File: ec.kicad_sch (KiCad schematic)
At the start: 51 parts, among them IC1 ADUM6010ARSZ, J1 EC, J2 Temperature, U1 ADuM1250, U2 ADS1115IDGS, U4 TPS60400DBV, U5 LM324, U6 MCP4017T-502E/LT

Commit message: Add title to all schematics pages
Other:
- title: (none) -> EC
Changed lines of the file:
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@@
 	(paper "A4")
 	(title_block
+		(title "EC")
 		(rev "1")
 	)

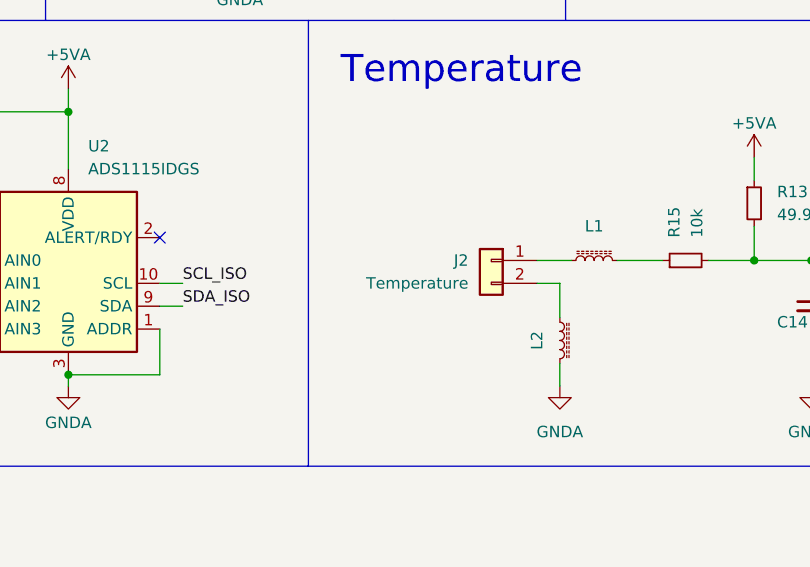
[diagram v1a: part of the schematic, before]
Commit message: Redesign board to fit within 102mm x 102mm
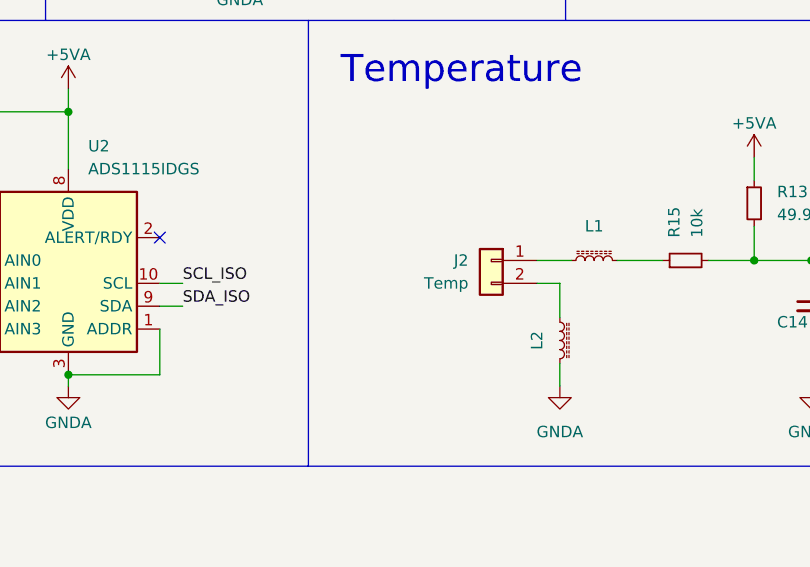
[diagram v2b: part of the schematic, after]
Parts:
- IC1, R1, U1, U2, U4: now left out of the parts list
- J2: value Temperature -> Temp
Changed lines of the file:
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@@
 		(unit 1)
 		(exclude_from_sim no)
-		(in_bom yes)
+		(in_bom no)
 		(on_board yes)
 		(dnp no)
@@
 		(unit 1)
 		(exclude_from_sim no)
-		(in_bom yes)
+		(in_bom no)
 		(on_board yes)
 		(dnp no)
@@
 		(unit 1)
 		(exclude_from_sim no)
-		(in_bom yes)
+		(in_bom no)
 		(on_board yes)
 		(dnp no)
@@
 		(unit 1)
 		(exclude_from_sim no)
-		(in_bom yes)
+		(in_bom no)
 		(on_board yes)
 		(dnp no)
@@
 			)
 		)
-		(property "Value" "Temperature"
+		(property "Value" "Temp"
 			(at 195.58 105.4099 0)
 			(effects
@@
 		(unit 1)
 		(exclude_from_sim no)
-		(in_bom yes)
+		(in_bom no)
 		(on_board yes)
 		(dnp no)

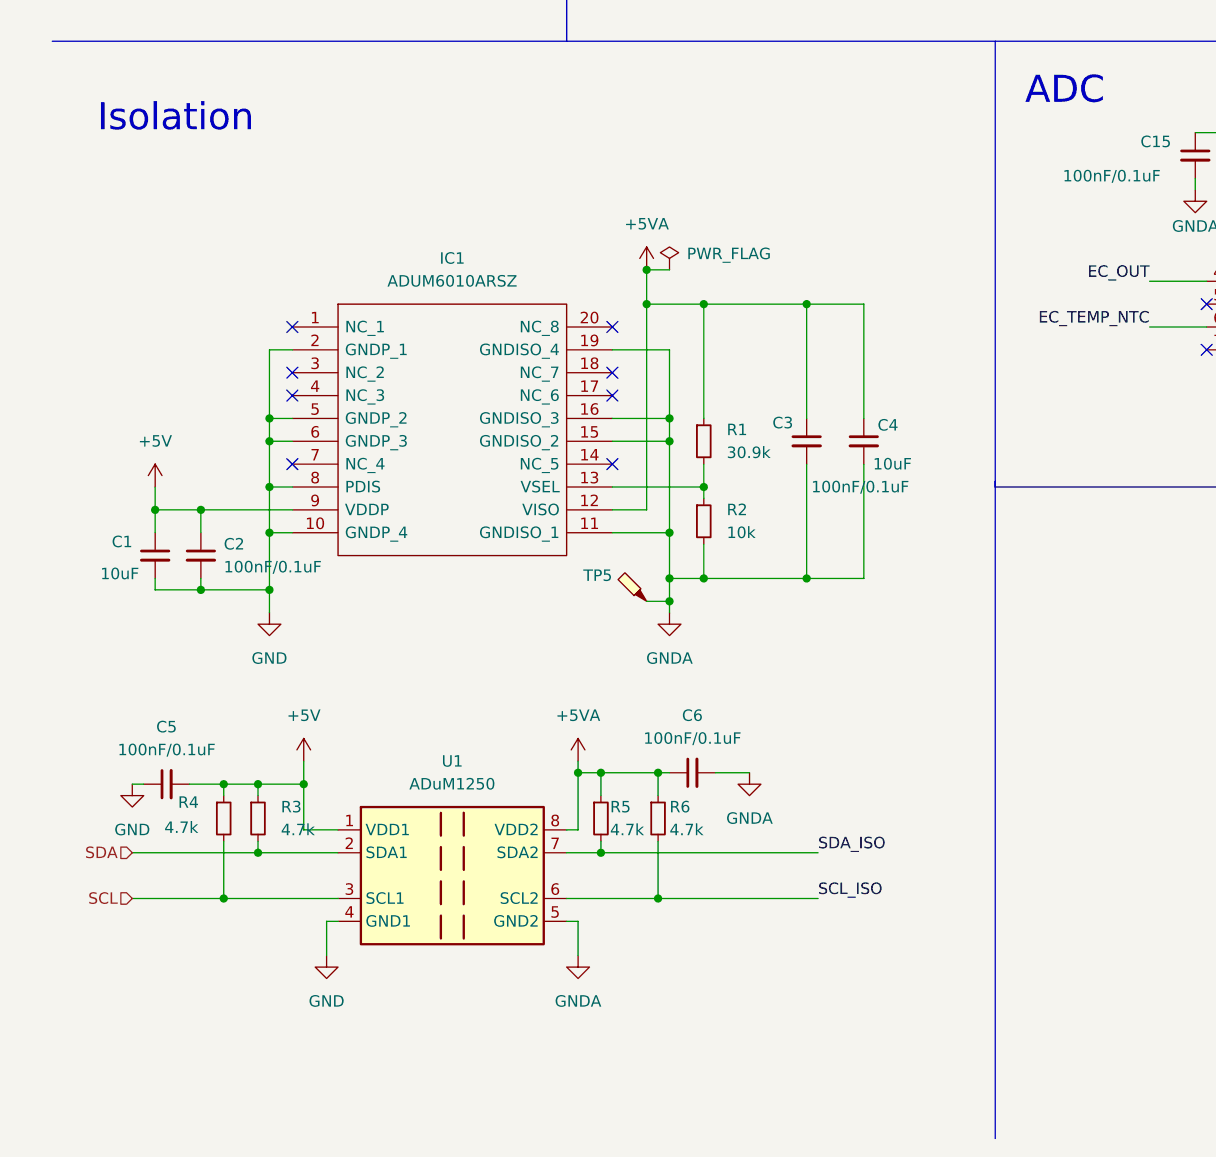
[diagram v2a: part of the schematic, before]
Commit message: Switch isolators to ADM3260
Change EC isolator.
See #1
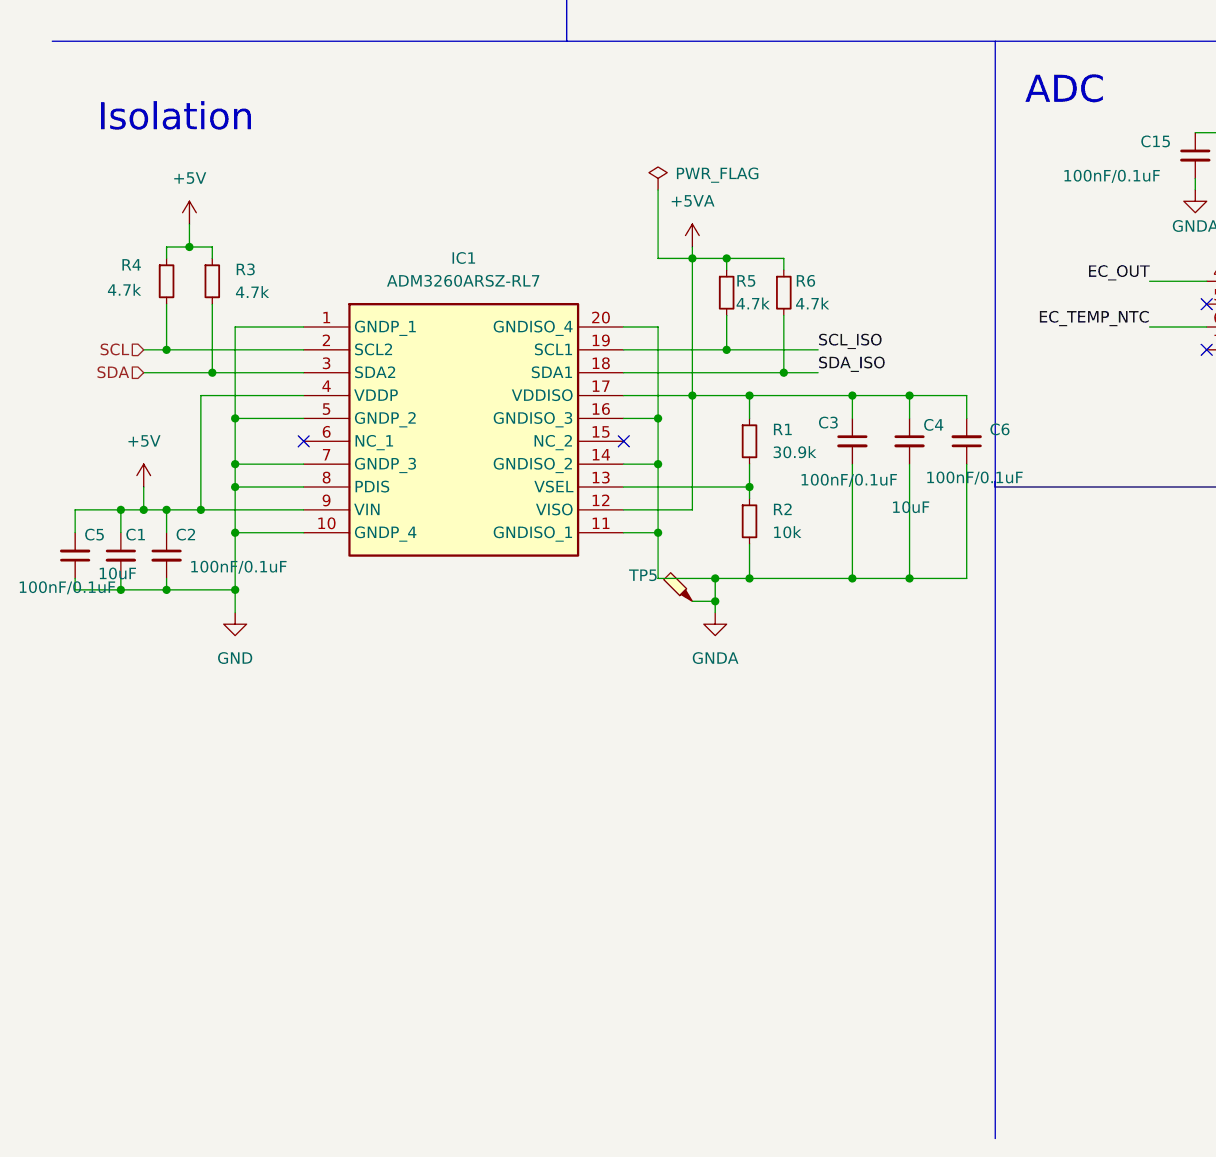
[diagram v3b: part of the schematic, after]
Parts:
- removed IC1: ADUM6010ARSZ, HydroponicFlowerControl:ADUM6010, symbol HydroponicFlowerControl:ADUM6010ARSZ
- removed U1: ADuM1250, Package_SO:SOIC-8_3.9x4.9mm_P1.27mm, symbol Isolator:ADuM1250
- added IC1: ADM3260ARSZ-RL7, HydroponicFlowerControl:SOP65P780X200-20N, symbol HydroponicFlowerControl:ADM3260ARSZ-RL7
- U6: JLCPCB Rotation Offset (none) -> -90
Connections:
- net +5V: now also IC1.4 (VDDP), IC1.9 (VIN)
- net +5VA: now also C6.2, IC1.12 (VISO), IC1.17 (VDDISO); no longer C6.1
- net GND: now also IC1.1 (GNDP_1), IC1.10 (GNDP_4), IC1.5 (GNDP_2), IC1.7 (GNDP_3), IC1.8 (PDIS)
- net GNDA: now also C6.1, IC1.11 (GNDISO_1), IC1.14 (GNDISO_2), IC1.16 (GNDISO_3), IC1.20 (GNDISO_4); no longer C6.2
- net SCL: now also IC1.2 (SCL2)
- net SCL_ISO: now also R5.2, IC1.19 (SCL1); no longer R6.2
- net SDA: now also IC1.3 (SDA2)
- net SDA_ISO: now also R6.2, IC1.18 (SDA1); no longer R5.2
- net at R1.2, R2.1: now also IC1.13 (VSEL)
- no-connect marks 11 -> 5
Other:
- moved on the sheet: C1, C2, C3, C4, C5, C6, R1, R2, R3, R4, R5, R6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

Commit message: Add disable signals for ec and ph
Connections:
- net GND: no longer IC1.8 (PDIS)
- new net DISABLE: IC1.8 (PDIS)
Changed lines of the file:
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@@
-	)
-	(junction
-		(at 33.02 125.73)
-		(diameter 0)
-		(color 0 0 0 0)
 	)
 	(junction
@@
 	(wire
 		(pts
-			(xy 33.02 125.73) (xy 33.02 130.81)
+			(xy 33.02 123.19) (xy 33.02 130.81)
 		)
 		(stroke
@@
 	(wire
 		(pts
-			(xy 33.02 125.73) (xy 40.64 125.73)
-		)
-		(stroke
-			(width 0)
-			(type default)
-		)
-	)
-	(wire
-		(pts
 			(xy 40.64 107.95) (xy 33.02 107.95)
 		)
@@
 		(pts
 			(xy 25.4 110.49) (xy 40.64 110.49)
-		)
-		(stroke
-			(width 0)
-			(type default)
-		)
-	)
-	(wire
-		(pts
-			(xy 33.02 123.19) (xy 33.02 125.73)
 		)
 		(stroke
@@
 		(fields_autoplaced yes)
 		(effects
+			(font
+				(size 1.27 1.27)
+			)
+			(justify right)
+		)
+	)
+	(hierarchical_label "DISABLE"
+		(shape input)
+		(at 40.64 125.73 180)
+		(fields_autoplaced yes)
+		(effects

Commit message: Fix manufaturing properties
Such as rotations
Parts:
- IC1, U2: JLCPCB Rotation Offset (none) -> 270; now in the parts list
- R1, U4: now in the parts list
- U6: JLCPCB Rotation Offset -90 -> 90
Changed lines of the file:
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@@
 		(unit 1)
 		(exclude_from_sim no)
-		(in_bom no)
+		(in_bom yes)
 		(on_board yes)
 		(dnp no)
@@
 			)
 		)
+		(property "JLCPCB Rotation Offset" "270"
+			(at 151.13 105.41 0)
+			(effects
+				(font
+					(size 1.27 1.27)
+				)
+				(hide yes)
+			)
+		)
 		(pin "3"
 		)
@@
 		(unit 1)
 		(exclude_from_sim no)
-		(in_bom no)
+		(in_bom yes)
 		(on_board yes)
 		(dnp no)
@@
 			)
 		)
+		(property "JLCPCB Rotation Offset" "270"
+			(at 40.64 107.95 0)
+			(effects
+				(font
+					(size 1.27 1.27)
+				)
+				(hide yes)
+			)
+		)
 		(pin "17"
 		)
@@
 		(unit 1)
 		(exclude_from_sim no)
-		(in_bom no)
+		(in_bom yes)
 		(on_board yes)
 		(dnp no)
@@
 		(unit 1)
 		(exclude_from_sim no)
-		(in_bom no)
+		(in_bom yes)
 		(on_board yes)
 		(dnp no)
@@
 			)
 		)
-		(property "JLCPCB Rotation Offset" "-90"
+		(property "JLCPCB Rotation Offset" "90"
 			(at 172.72 62.23 0)
 			(effects

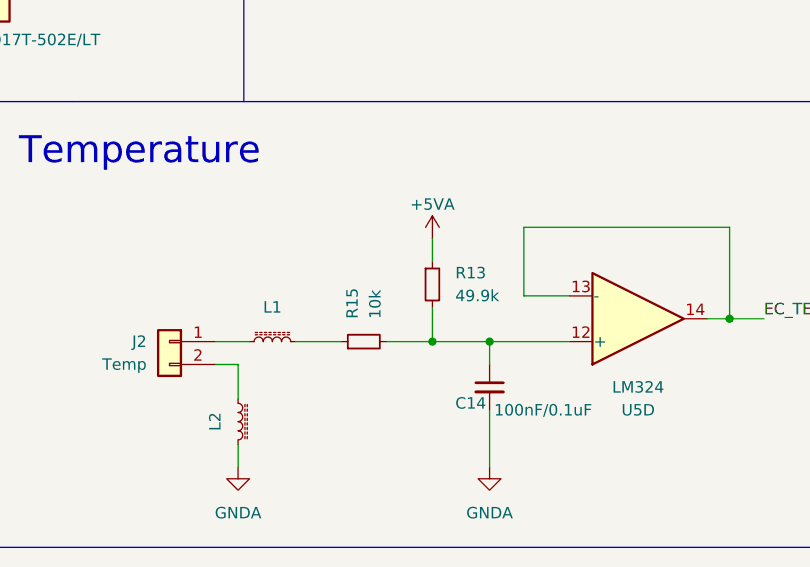
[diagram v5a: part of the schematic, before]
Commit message: Move R15 and R48 to the right side of the divider
Closes #6
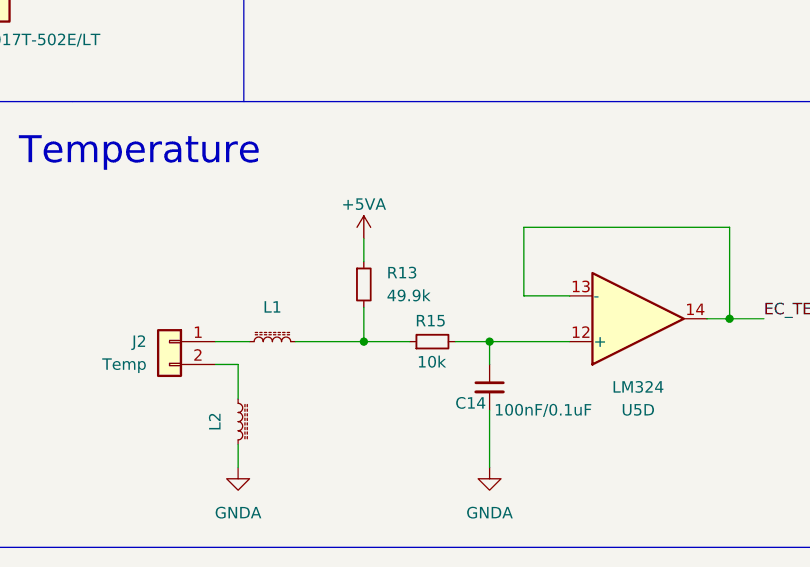
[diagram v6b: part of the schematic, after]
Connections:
- net at L1.2, R15.1: now also R13.2
- net at C14.1, R15.2, U5.12 (+): no longer R13.2
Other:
- moved on the sheet: R13, R15
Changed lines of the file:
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@@
 	)
 	(junction
+		(at 219.71 102.87)
+		(diameter 0)
+		(color 0 0 0 0)
+	)
+	(junction
 		(at 93.98 113.03)
 		(diameter 0)
@@
 	)
 	(junction
-		(at 227.33 102.87)
-		(diameter 0)
-		(color 0 0 0 0)
-	)
-	(junction
 		(at 245.11 41.91)
 		(diameter 0)
@@
 	(wire
 		(pts
-			(xy 227.33 102.87) (xy 233.68 102.87)
-		)
-		(stroke
-			(width 0)
-			(type default)
-		)
-	)
-	(wire
-		(pts
 			(xy 151.13 83.82) (xy 151.13 86.36)
 		)
@@
 	(wire
 		(pts
-			(xy 222.25 102.87) (xy 227.33 102.87)
-		)
-		(stroke
-			(width 0)
-			(type default)
-		)
-	)
-	(wire
-		(pts
 			(xy 101.6 135.89) (xy 90.17 135.89)
 		)
@@
 	(wire
 		(pts
-			(xy 227.33 91.44) (xy 227.33 93.98)
+			(xy 219.71 91.44) (xy 219.71 93.98)
 		)
 		(stroke
@@
 	(wire
 		(pts
-			(xy 212.09 102.87) (xy 217.17 102.87)
+			(xy 212.09 102.87) (xy 219.71 102.87)
 		)
 		(stroke
@@
 	(wire
 		(pts
-			(xy 227.33 102.87) (xy 227.33 99.06)
+			(xy 105.41 52.07) (xy 109.22 52.07)
 		)
 		(stroke
@@
 	(wire
 		(pts
-			(xy 105.41 52.07) (xy 109.22 52.07)
+			(xy 237.49 90.17) (xy 237.49 97.79)
 		)
 		(stroke
@@
 	(wire
 		(pts
-			(xy 237.49 90.17) (xy 237.49 97.79)
+			(xy 160.02 62.23) (xy 162.56 62.23)
 		)
 		(stroke
@@
 	(wire
 		(pts
-			(xy 160.02 62.23) (xy 162.56 62.23)
+			(xy 219.71 102.87) (xy 219.71 99.06)
 		)
 		(stroke
@@
 	(wire
 		(pts
+			(xy 219.71 102.87) (xy 224.79 102.87)
+		)
+		(stroke
+			(width 0)
+			(type default)
+		)
+	)
+	(wire
+		(pts
 			(xy 160.02 59.69) (xy 162.56 59.69)
 		)
@@
 	(wire
 		(pts
+			(xy 229.87 102.87) (xy 233.68 102.87)
+		)
+		(stroke
+			(width 0)
+			(type default)
+		)
+	)
+	(wire
+		(pts
 			(xy 102.87 39.37) (xy 107.95 39.37)
 		)
@@
 	(symbol
 		(lib_id "Device:R_Small")
-		(at 219.71 102.87 90)
+		(at 227.33 102.87 90)
 		(unit 1)
 		(exclude_from_sim no)
@@
 		(dnp no)
 		(property "Reference" "R15"
-			(at 218.4399 100.33 0)
+			(at 228.854 100.584 90)
 			(effects
 				(font
@@
 		)
 		(property "Value" "10k"
-			(at 220.9799 100.33 0)
+			(at 228.854 105.156 90)
 			(effects
 				(font
@@
 		)
 		(property "Footprint" "Resistor_SMD:R_0603_1608Metric"
-			(at 219.71 102.87 0)
+			(at 227.33 102.87 0)
 			(effects
 				(font
@@
 		)
 		(property "Datasheet" "~"
-			(at 219.71 102.87 0)
+			(at 227.33 102.87 0)
 			(effects
 				(font
@@
 		)
 		(property "Description" "Resistor, small symbol"
-			(at 219.71 102.87 0)
+			(at 227.33 102.87 0)
 			(effects
 				(font
@@
 		)
 		(property "LCSC alt" ""
-			(at 219.71 102.87 0)
+			(at 227.33 102.87 0)
 			(effects
 				(font
@@
 		)
 		(property "LCSC" "C25804"
-			(at 219.71 102.87 0)
+			(at 227.33 102.87 0)
 			(effects
 				(font
@@
 	(symbol
 		(lib_id "power:+5VA")
-		(at 227.33 91.44 0)
+		(at 219.71 91.44 0)
 		(unit 1)
 		(exclude_from_sim no)
@@
 		(dnp no)
 		(property "Reference" "#PWR026"
-			(at 227.33 95.25 0)
+			(at 219.71 95.25 0)
 			(effects
 				(font
@@
 		)
 		(property "Value" "+5VA"
-			(at 227.33 87.63 0)
+			(at 219.71 87.63 0)
 			(effects
 				(font
@@
 		)
 		(property "Footprint" ""
-			(at 227.33 91.44 0)
+			(at 219.71 91.44 0)
 			(effects
 				(font
@@
 		)
 		(property "Datasheet" ""
-			(at 227.33 91.44 0)
+			(at 219.71 91.44 0)
 			(effects
 				(font
@@
 		)
 		(property "Description" "Power symbol creates a global label with name \"+5VA\""
-			(at 227.33 91.44 0)
+			(at 219.71 91.44 0)
 			(effects
 				(font
@@
 	(symbol
 		(lib_id "Device:R_Small")
-		(at 227.33 96.52 0)
+		(at 219.71 96.52 0)
 		(unit 1)
 		(exclude_from_sim no)
@@
 		(dnp no)
 		(property "Reference" "R13"
-			(at 229.87 95.2499 0)
+			(at 222.25 95.2499 0)
 			(effects
 				(font
@@
 		)
 		(property "Value" "49.9k"
-			(at 229.87 97.7899 0)
+			(at 222.25 97.7899 0)
 			(effects
 				(font
@@
 		)
 		(property "Footprint" "Resistor_SMD:R_0603_1608Metric"
-			(at 227.33 96.52 0)
+			(at 219.71 96.52 0)
 			(effects
 				(font
@@
 		)
 		(property "Datasheet" "~"
-			(at 227.33 96.52 0)
+			(at 219.71 96.52 0)
 			(effects
 				(font
@@
 		)
 		(property "Description" "Resistor, small symbol"
-			(at 227.33 96.52 0)
+			(at 219.71 96.52 0)
 			(effects
 				(font
@@
 		)
 		(property "LCSC alt" ""
-			(at 227.33 96.52 0)
+			(at 219.71 96.52 0)
 			(effects
 				(font
@@
 		)
 		(property "LCSC" "C23184"
-			(at 227.33 96.52 0)
+			(at 219.71 96.52 0)
 			(effects
 				(font

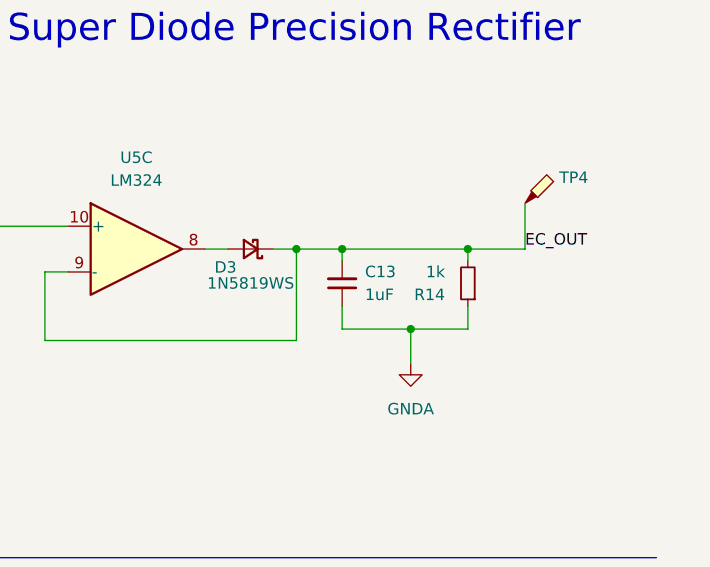
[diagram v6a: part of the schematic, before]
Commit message: Optimize EC RC filter
Closes #5
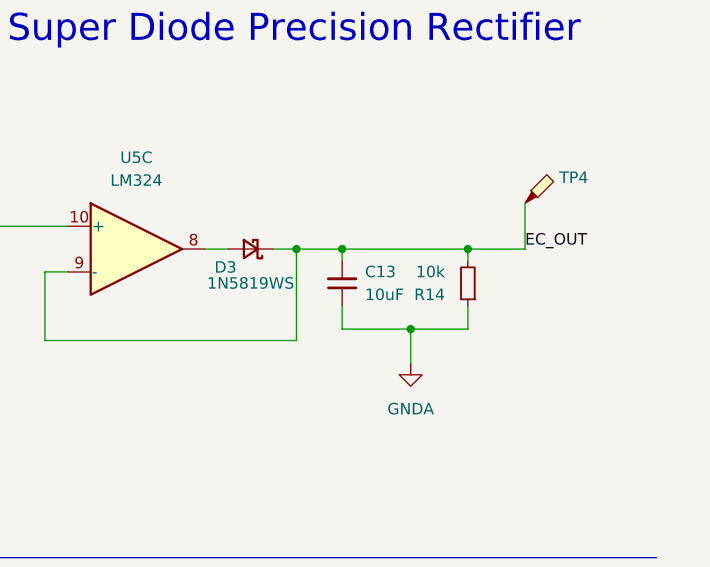
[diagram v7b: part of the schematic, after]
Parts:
- C13: value 1uF -> 10uF; footprint Capacitor_SMD:C_0603_1608Metric -> Capacitor_SMD:C_0805_2012Metric; LCSC C15849 -> C15850
- R14: value 1k -> 10k; LCSC C21190 -> C25804
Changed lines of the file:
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@@
 			)
 		)
-		(property "Value" "1uF"
+		(property "Value" "10uF"
 			(at 252.73 46.9835 0)
 			(effects
@@
 			)
 		)
-		(property "Footprint" "Capacitor_SMD:C_0603_1608Metric"
+		(property "Footprint" "Capacitor_SMD:C_0805_2012Metric"
 			(at 250.19 45.72 0)
 			(effects
@@
 			)
 		)
-		(property "LCSC" "C15849"
-			(at 250.19 45.72 0)
-			(effects
-				(font
-					(size 1.27 1.27)
-				)
-				(hide yes)
-			)
-		)
-		(property "LCSC alt" ""
+		(property "LCSC" "C15850"
 			(at 250.19 45.72 0)
 			(effects
@@
 			)
 		)
-		(property "Value" "1k"
+		(property "Value" "10k"
 			(at 261.62 44.4501 0)
 			(effects
@@
 			)
 		)
-		(property "LCSC" "C21190"
+		(property "LCSC" "C25804"
 			(at 264.16 45.72 0)
 			(effects
@@
 			(at 99.06 55.88 0)
 			(effects
-				(font
-					(size 1.27 1.27)
-				)
-				(hide yes)
-			)
-		)
-		(property "LCSC alt" ""
-			(at 99.06 55.88 0)
-			(effects

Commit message: Add testpoints for power and gnd
Closes #3
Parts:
- TP4: value TestPoint_Small -> EC
- TP5: value GND_ISO -> GNDA; footprint TestPoint:TestPoint_Pad_D1.0mm -> TestPoint:TestPoint_Loop_D1.80mm_Drill1.0mm_Beaded
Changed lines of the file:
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@@
 			)
 		)
-		(property "Value" "GND_ISO"
+		(property "Value" "GNDA"
 			(at 80.01 138.1124 0)
 			(effects
@@
 			)
 		)
-		(property "Footprint" "TestPoint:TestPoint_Pad_D1.0mm"
+		(property "Footprint" "TestPoint:TestPoint_Loop_D1.80mm_Drill1.0mm_Beaded"
 			(at 78.74 138.43 0)
 			(effects
@@
 			)
 		)
-		(property "LCSC alt" ""
+		(property "LCSC" ""
 			(at 83.82 138.43 0)
 			(effects
@@
 			)
 		)
-		(property "Value" "TestPoint_Small"
+		(property "Value" "EC"
 			(at 274.32 36.5124 0)
 			(effects
